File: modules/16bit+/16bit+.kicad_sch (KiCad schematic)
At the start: 52 parts, among them J1 Conn_01x08_Socket, J2 Conn_01x08_Socket, J5 USB_C_Receptacle_USB2.0_14P, SW1 K2-1808SN-A4SW-01, SW2 K2-1808SN-A4SW-01, SW3 K2-1808SN-A4SW-01, U1 RP2350_60QFN, U2 W25Q128JVS, U3 MCP6002-xSN, U5 PSRAM, Y1 ABM8-272-T3

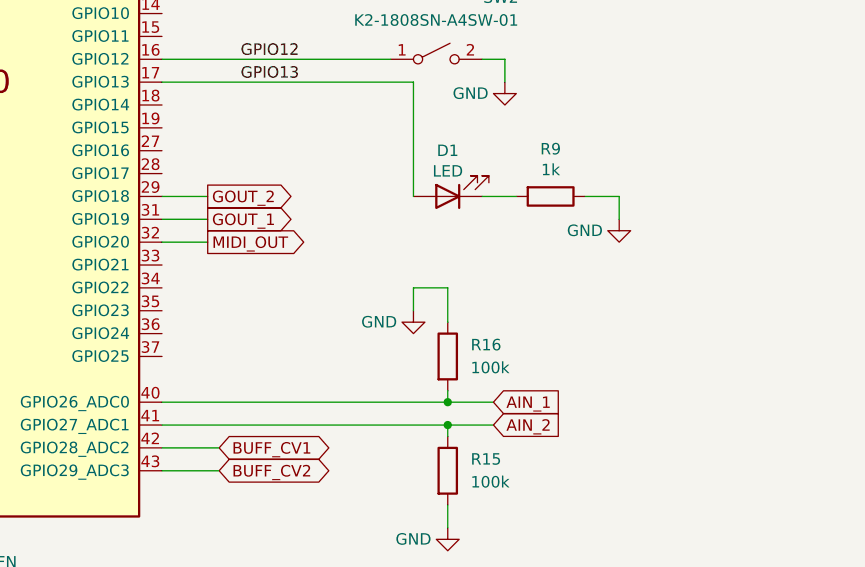
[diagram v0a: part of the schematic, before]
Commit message: Detect 16bit+ at runtime via IO21
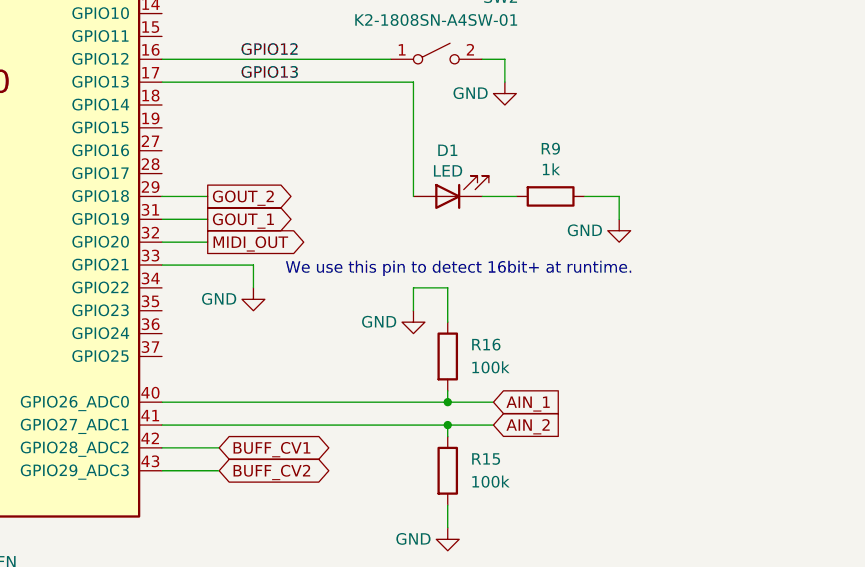
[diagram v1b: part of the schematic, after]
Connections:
- net GND: now also U1.33 (GPIO21)
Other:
- note added: "We use this pin to detect 16bit+ at runtime."
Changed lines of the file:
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@@
 		)
 	)
+	(text "We use this pin to detect 16bit+ at runtime."
+		(exclude_from_sim no)
+		(at 262.89 165.608 0)
+		(effects
+			(font
+				(size 1.27 1.27)
+			)
+		)
+	)
 	(text "12MHz Crystal"
 		(exclude_from_sim no)
@@
 	(wire
 		(pts
+			(xy 229.87 165.1) (xy 240.03 165.1)
+		)
+		(stroke
+			(width 0)
+			(type default)
+		)
+	)
+	(wire
+		(pts
 			(xy 92.71 383.54) (xy 100.33 383.54)
 		)
@@
 	(wire
 		(pts
+			(xy 240.03 165.1) (xy 240.03 167.64)
+		)
+		(stroke
+			(width 0)
+			(type default)
+		)
+	)
+	(wire
+		(pts
 			(xy 246.38 69.85) (xy 246.38 72.39)
 		)
@@
 					(unit 1)
 				)
+			)
+		)
+	)
+	(symbol
+		(lib_id "power:GND")
+		(at 240.03 167.64 0)
+		(unit 1)
+		(exclude_from_sim no)
+		(in_bom yes)
+		(on_board yes)
+		(dnp no)
+		(property "Reference" "#PWR026"
+			(at 240.03 173.99 0)
+			(effects
+				(font
+					(size 1.27 1.27)
+				)
+				(hide yes)
+			)
+		)
+		(property "Value" "GND"
+			(at 236.22 168.91 0)
+			(effects
+				(font
+					(size 1.27 1.27)
+				)
+			)
+		)
+		(property "Footprint" ""
+			(at 240.03 167.64 0)
+			(effects
+				(font
+					(size 1.27 1.27)
+				)
+				(hide yes)
+			)
+		)
+		(property "Datasheet" ""
+			(at 240.03 167.64 0)
+			(effects
+				(font
+					(size 1.27 1.27)
+				)
+				(hide yes)
+			)
+		)
+		(property "Description" ""
+			(at 240.03 167.64 0)
+			(effects
+				(font
+					(size 1.27 1.27)
+				)
+				(hide yes)
+			)
+		)
+		(pin "1"
+		)
+		(instances
+			(project "16bit+"
+				(path "/94683f5c-9cd9-448e-be96-9792537b5cb8"
+					(reference "#PWR026")
+					(unit 1)
+				)

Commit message: Finalize the schematics
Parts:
- added C21, C22, C26, C34, C36, C39: 0.1uf, Capacitor_SMD:C_0402_1005Metric, symbol Device:C_Small
- added C23, C25, C30, C31: 1uf, Capacitor_SMD:C_0402_1005Metric, symbol Device:C_Small
- added C27, C33, C35, C37, C38, C5: 10uf, Capacitor_SMD:C_0402_1005Metric, symbol Device:C_Small
- added R13, R17: 1k, Resistor_SMD:R_0402_1005Metric, symbol Device:R_Small
- added R19, R20, R21, R22, R23: 33, Resistor_SMD:R_0402_1005Metric, symbol Device:R_Small
- added R24, R25: 10k, Resistor_SMD:R_0402_1005Metric, symbol Device:R_Small
- added U4: ~, Package_DFN_QFN:QFN-28-1EP_4x4mm_P0.45mm_EP2.4x2.4mm_ThermalVias, symbol BreadModular_Symbols:ES8388
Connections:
- net +3V3: now also C21.1, C22.1, C26.1, C37.1, C38.1, C39.1, C5.1, R24.2, R25.2, U4.16 (HPVDD), U4.17 (AVDD), U4.2 (DVDD), U4.3 (PVDD)
- net AIN_1: now also R15.1, C31.2; no longer R16.2, U1.40 (GPIO26_ADC0)
- net AIN_2: now also R16.1, C30.2; no longer R15.1, U1.41 (GPIO27_ADC1)
- net AOUT_1: now also R17.1
- net AOUT_2: now also R13.1
- net GND: now also R16.2, C21.2, C22.2, C26.2, C27.1, C33.2, C34.2, C35.2, C36.2, C37.2, C38.2, C39.2, C5.2, U4.13 (HPGND), U4.18 (AGND), U4.26 (CE), U4.29 (Thermal_Vias), U4.4 (DGND); no longer R16.1
- net SCLK: now reaches U1.10 (GPIO7)
- net SCLK: now also R20.1
- net DSDIN: now reaches U1.12 (GPIO8)
- net DSDIN: now also R21.1
- net LRCK: now reaches U1.13 (GPIO9)
- net LRCK: now also R22.1
- net ASDOUT: now reaches U1.14 (GPIO10)
- net ASDOUT: now also R23.1
- net CDATA: now reaches U1.4 (GPIO2)
- net CDATA: now also R24.1, U4.27 (CDATA)
- net CCLK: now reaches U1.5 (GPIO3)
- net CCLK: now also R25.1, U4.28 (CCLK)
- net MCLK: now reaches U1.9 (GPIO6)
- net MCLK: now also R19.1
- new net: C23.1, R13.2
- new net: C30.1, U4.23 (RIN1)
- new net: C23.2, U4.11 (ROUT1)
- new net: R20.2, U4.5 (SCLK)
- new net: R22.2, U4.7 (LRCK)
- new net: R19.2, U4.1 (MCLK)
- new net: C33.1, C34.1, U4.20 (VMID)
- new net: C25.1, R17.2
- new net: C27.2, U4.10 (VREF)
- new net: C31.1, U4.24 (LIN1)
- new net: R23.2, U4.8 (ASDOUT)
- new net: C35.1, C36.1, U4.19 (ADCVREF)
- new net: C25.2, U4.12 (LOUT1)
- new net: R21.2, U4.6 (DSDIN)
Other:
- note added: "## Audio Codec ES8388"
- note removed: "## DAC 16-bit PT8211 DAC."
- moved on the sheet: R15, R16

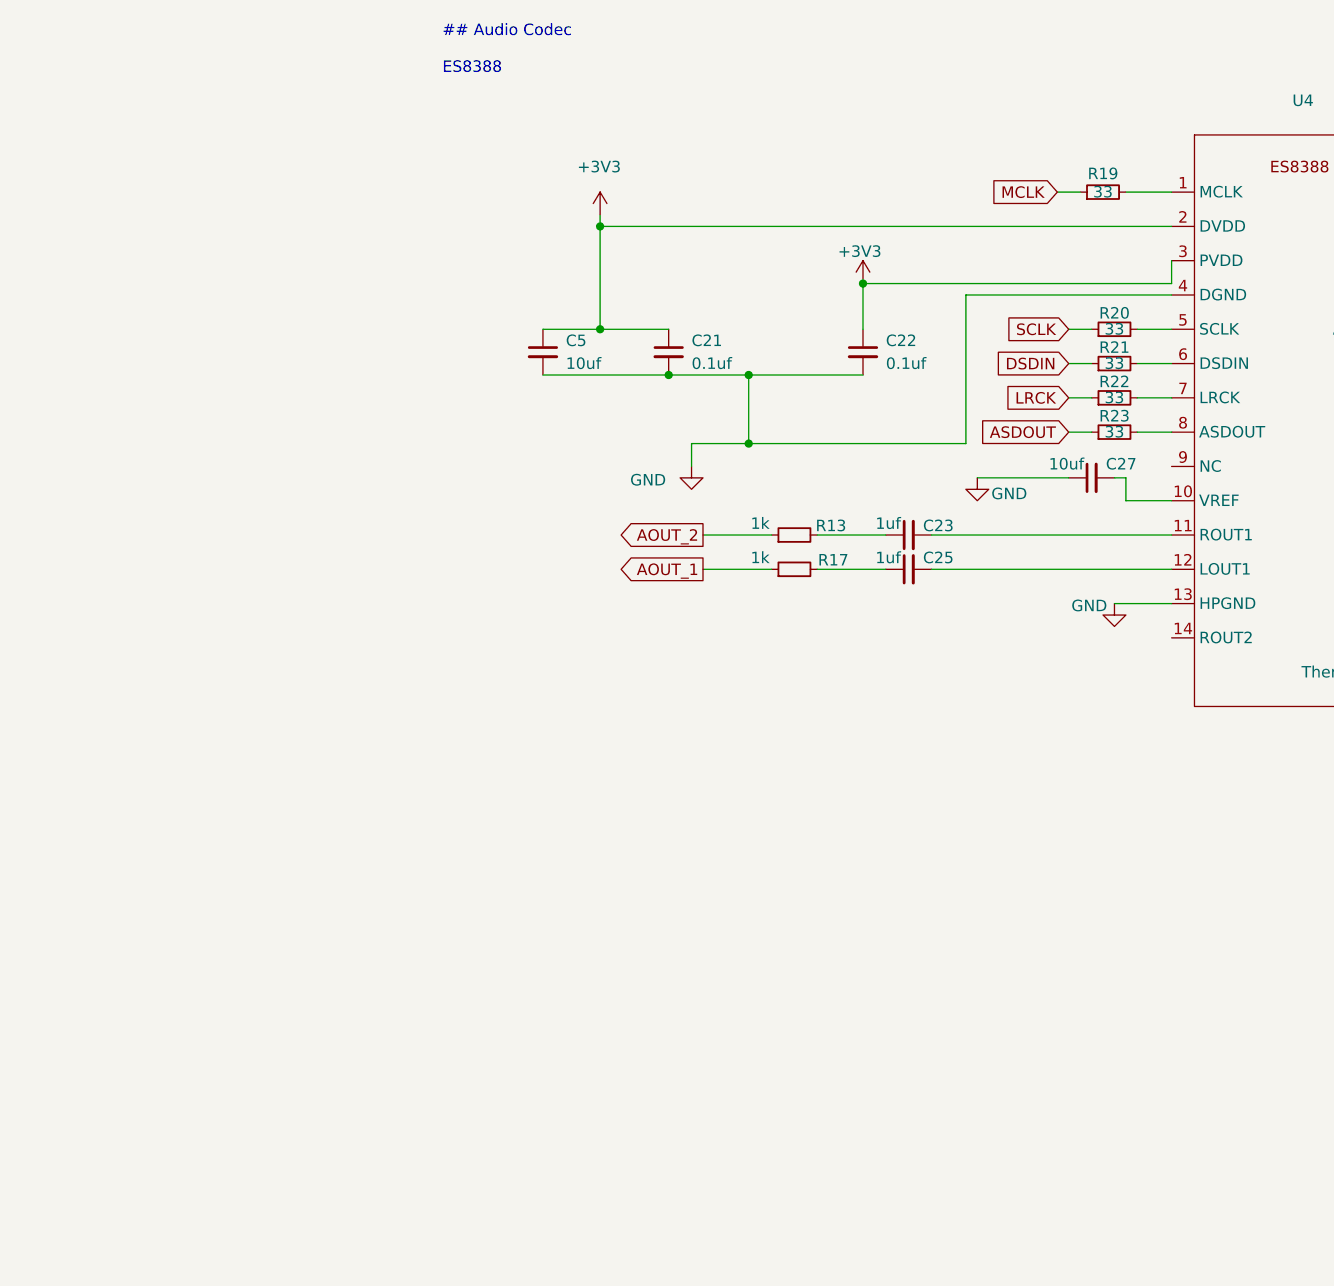
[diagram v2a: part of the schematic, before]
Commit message: 16bit+: add external crystal to generate MCLK
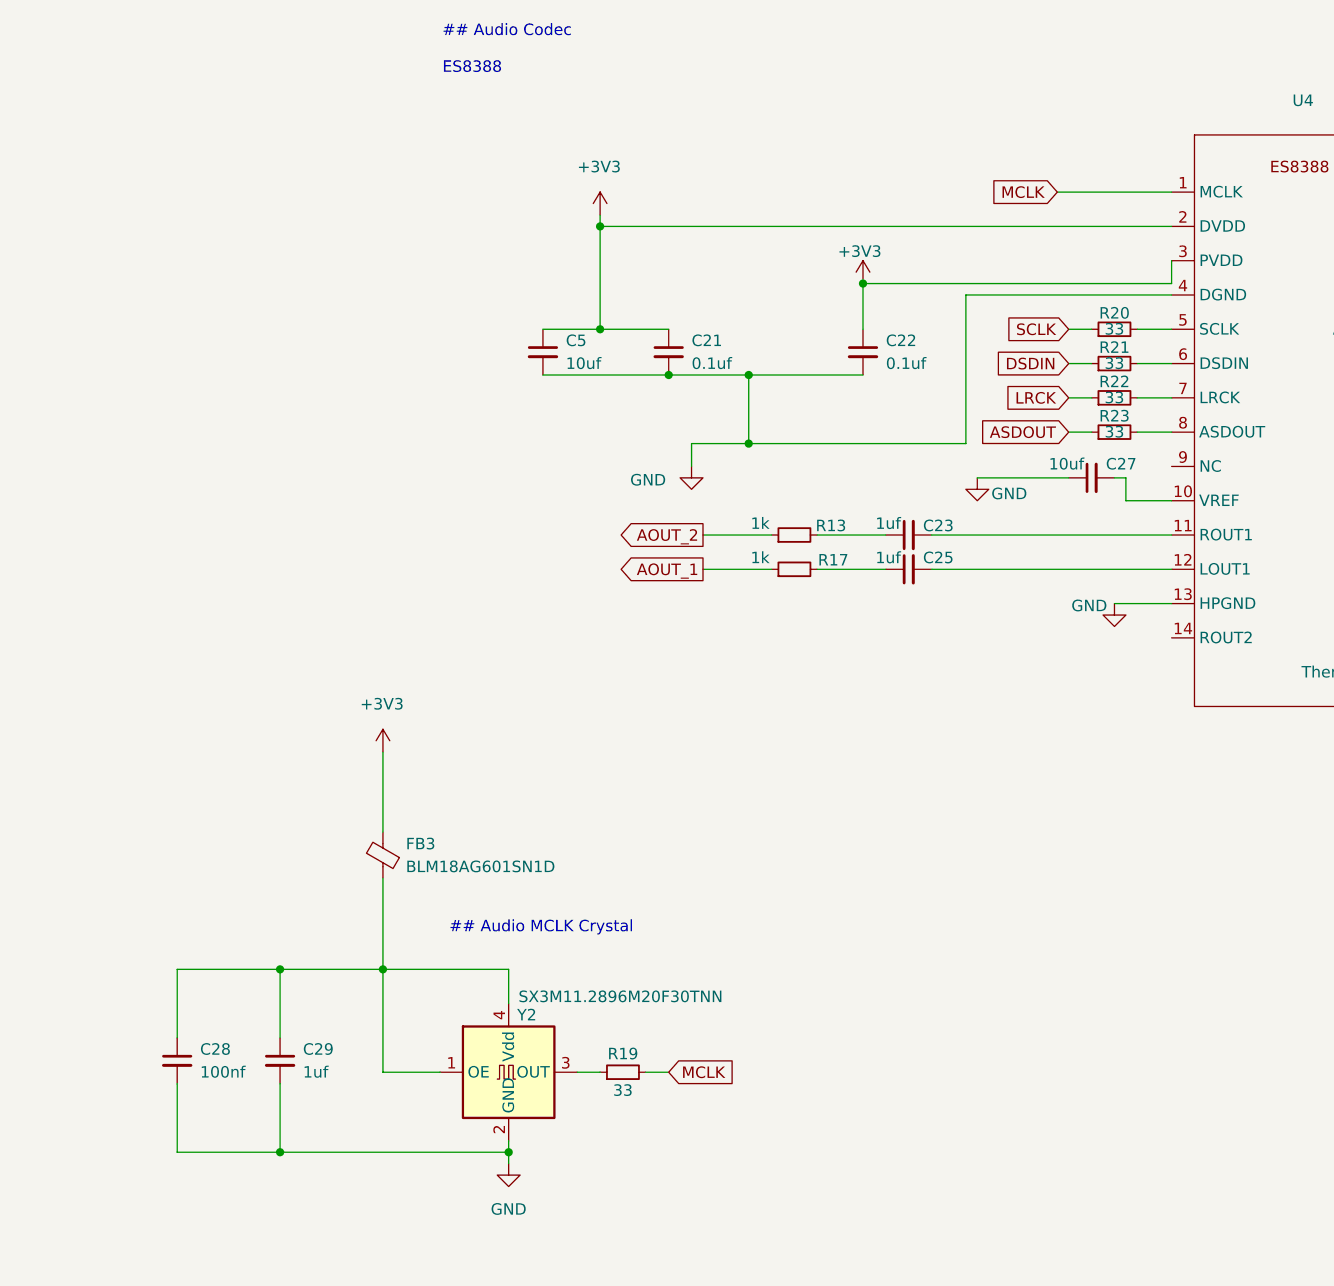
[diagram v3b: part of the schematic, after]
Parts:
- added C28: 100nf, Capacitor_SMD:C_0402_1005Metric, symbol Device:C_Small
- added C29: 1uf, Capacitor_SMD:C_0402_1005Metric, symbol Device:C_Small
- added FB3: BLM18AG601SN1D, Capacitor_SMD:C_0603_1608Metric, symbol Device:FerriteBead_Small
- added Y2: SX3M11.2896M20F30TNN, Oscillator:Oscillator_SMD_SiT_PQFN-4Pin_3.2x2.5mm, symbol Oscillator:SiT8008xx-2x-xxE
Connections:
- net +3V3: now also FB3.2
- net GND: now also C28.2, C29.2, Y2.2 (GND)
- net MCLK: now also R19.2, U4.1 (MCLK); no longer R19.1
- new net: C28.1, C29.1, FB3.1, Y2.1 (OE), Y2.4 (Vdd)
- new net: R19.1, Y2.3 (OUT)
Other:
- note added: "## Audio MCLK Crystal"
- moved on the sheet: R19
